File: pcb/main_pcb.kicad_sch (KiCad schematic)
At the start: 43 parts, among them J1 Conn_01x06_Socket, J4 USB_C_Receptacle_USB2.0, Q1 Si2323DS, SW1 SW_Push, SW2 SW_Push, SW3 SW_Push, U1 ESP32-H2-MINI-1, U2 LM5165Y, Y1 32.768KHz

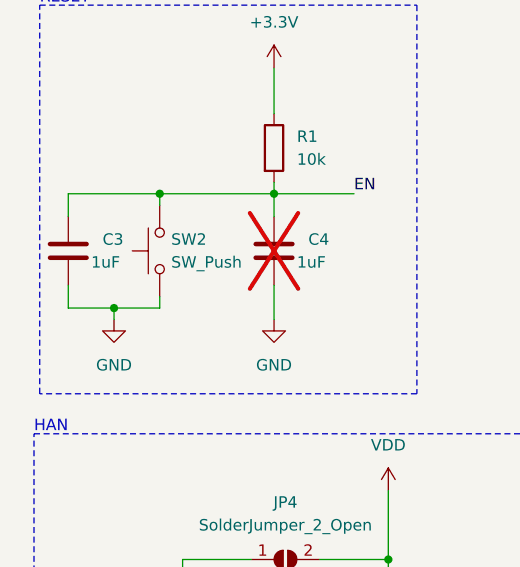
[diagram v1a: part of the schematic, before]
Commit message: Remove redundant capacitor from reset circuit
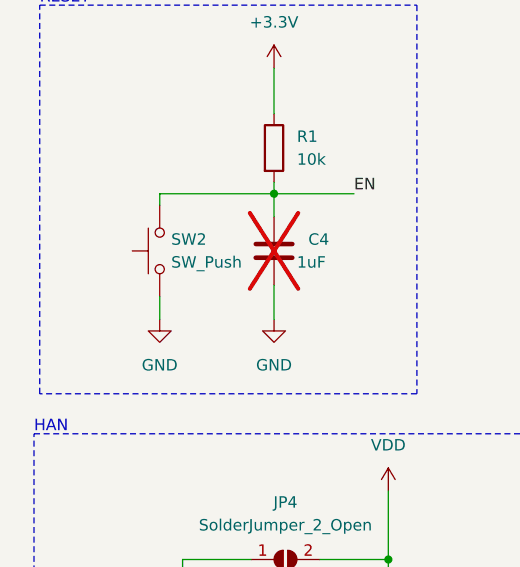
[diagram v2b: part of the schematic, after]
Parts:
- removed C3: 1uF, Capacitor_SMD:C_1206_3216Metric_Pad1.33x1.80mm_HandSolder, symbol Device:C
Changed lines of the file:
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@@
   (junction (at 165.1 176.53) (diameter 0) (color 0 0 0 0)
   )
-  (junction (at 35.56 139.7) (diameter 0) (color 0 0 0 0)
-  )
   (junction (at 111.76 72.39) (diameter 0) (color 0 0 0 0)
   )
@@
   )
   (junction (at 68.58 63.5) (diameter 0) (color 0 0 0 0)
-  )
-  (junction (at 30.48 152.4) (diameter 0) (color 0 0 0 0)
   )
   (junction (at 55.88 83.82) (diameter 0) (color 0 0 0 0)
@@
     (stroke (width 0) (type default))
   )
-  (wire (pts (xy 25.4 142.24) (xy 25.4 139.7))
-    (stroke (width 0) (type default))
-  )
   (wire (pts (xy 198.12 162.56) (xy 198.12 176.53))
     (stroke (width 0) (type default))
@@
     (stroke (width 0) (type default))
   )
-  (wire (pts (xy 25.4 139.7) (xy 35.56 139.7))
-    (stroke (width 0) (type default))
-  )
   (wire (pts (xy 250.19 134.62) (xy 256.54 134.62))
     (stroke (width 0) (type default))
@@
     (stroke (width 0) (type default))
   )
-  (wire (pts (xy 35.56 152.4) (xy 35.56 151.13))
+  (wire (pts (xy 35.56 151.13) (xy 35.56 153.67))
     (stroke (width 0) (type default))
   )
@@
     (stroke (width 0) (type default))
   )
-  (wire (pts (xy 30.48 152.4) (xy 35.56 152.4))
-    (stroke (width 0) (type default))
-  )
   (wire (pts (xy 219.71 181.61) (xy 219.71 190.5))
     (stroke (width 0) (type default))
@@
     (stroke (width 0) (type default))
   )
-  (wire (pts (xy 25.4 152.4) (xy 30.48 152.4))
-    (stroke (width 0) (type default))
-  )
   (wire (pts (xy 118.11 53.34) (xy 124.46 53.34))
     (stroke (width 0) (type default))
@@
     (stroke (width 0) (type default))
   )
-  (wire (pts (xy 25.4 149.86) (xy 25.4 152.4))
-    (stroke (width 0) (type default))
-  )
   (wire (pts (xy 201.93 189.23) (xy 191.77 189.23))
     (stroke (width 0) (type default))
@@
   )
   (wire (pts (xy 173.99 199.39) (xy 173.99 200.66))
-    (stroke (width 0) (type default))
-  )
-  (wire (pts (xy 30.48 152.4) (xy 30.48 153.67))
     (stroke (width 0) (type default))
   )
@@
     )
   )
-  (symbol (lib_id "power:GND") (at 30.48 153.67 0) (unit 1)
-    (in_bom yes) (on_board yes) (dnp no) (fields_autoplaced)
-    (property "Reference" "#PWR08" (at 30.48 160.02 0)
-      (effects (font (size 1.27 1.27)) hide)
-    )
-    (property "Value" "GND" (at 30.48 158.75 0)
-      (effects (font (size 1.27 1.27)))
-    )
-    (property "Footprint" "" (at 30.48 153.67 0)
-      (effects (font (size 1.27 1.27)) hide)
-    )
-    (property "Datasheet" "" (at 30.48 153.67 0)
+  (symbol (lib_id "power:GND") (at 35.56 153.67 0) (unit 1)
+    (in_bom yes) (on_board yes) (dnp no) (fields_autoplaced)
+    (property "Reference" "#PWR08" (at 35.56 160.02 0)
+      (effects (font (size 1.27 1.27)) hide)
+    )
+    (property "Value" "GND" (at 35.56 158.75 0)
+      (effects (font (size 1.27 1.27)))
+    )
+    (property "Footprint" "" (at 35.56 153.67 0)
+      (effects (font (size 1.27 1.27)) hide)
+    )
+    (property "Datasheet" "" (at 35.56 153.67 0)
       (effects (font (size 1.27 1.27)) hide)
     )
@@
         )
       )
-    )
-  )
-  (symbol (lib_id "Device:C") (at 25.4 146.05 0) (unit 1)
-    (in_bom yes) (on_board yes) (dnp no)
-    (property "Reference" "C3" (at 29.21 144.78 0)
-      (effects (font (size 1.27 1.27)) (justify left))
-    )
-    (property "Value" "1uF" (at 27.94 147.32 0)
-      (effects (font (size 1.27 1.27)) (justify left))
-    )
-    (property "Footprint" "Capacitor_SMD:C_1206_3216Metric_Pad1.33x1.80mm_HandSolder" (at 26.3652 149.86 0)
-      (effects (font (size 1.27 1.27)) hide)
-    )
-    (property "Datasheet" "~" (at 25.4 146.05 0)
-      (effects (font (size 1.27 1.27)) hide)
-    )
-    (pin "2")
-    (pin "1")
-    (instances
-      (project "main_pcb"
-        (path "/6204b7c2-8814-41ee-9243-5078f55f08d4"
-          (reference "C3") (unit 1)
-        )
-      )

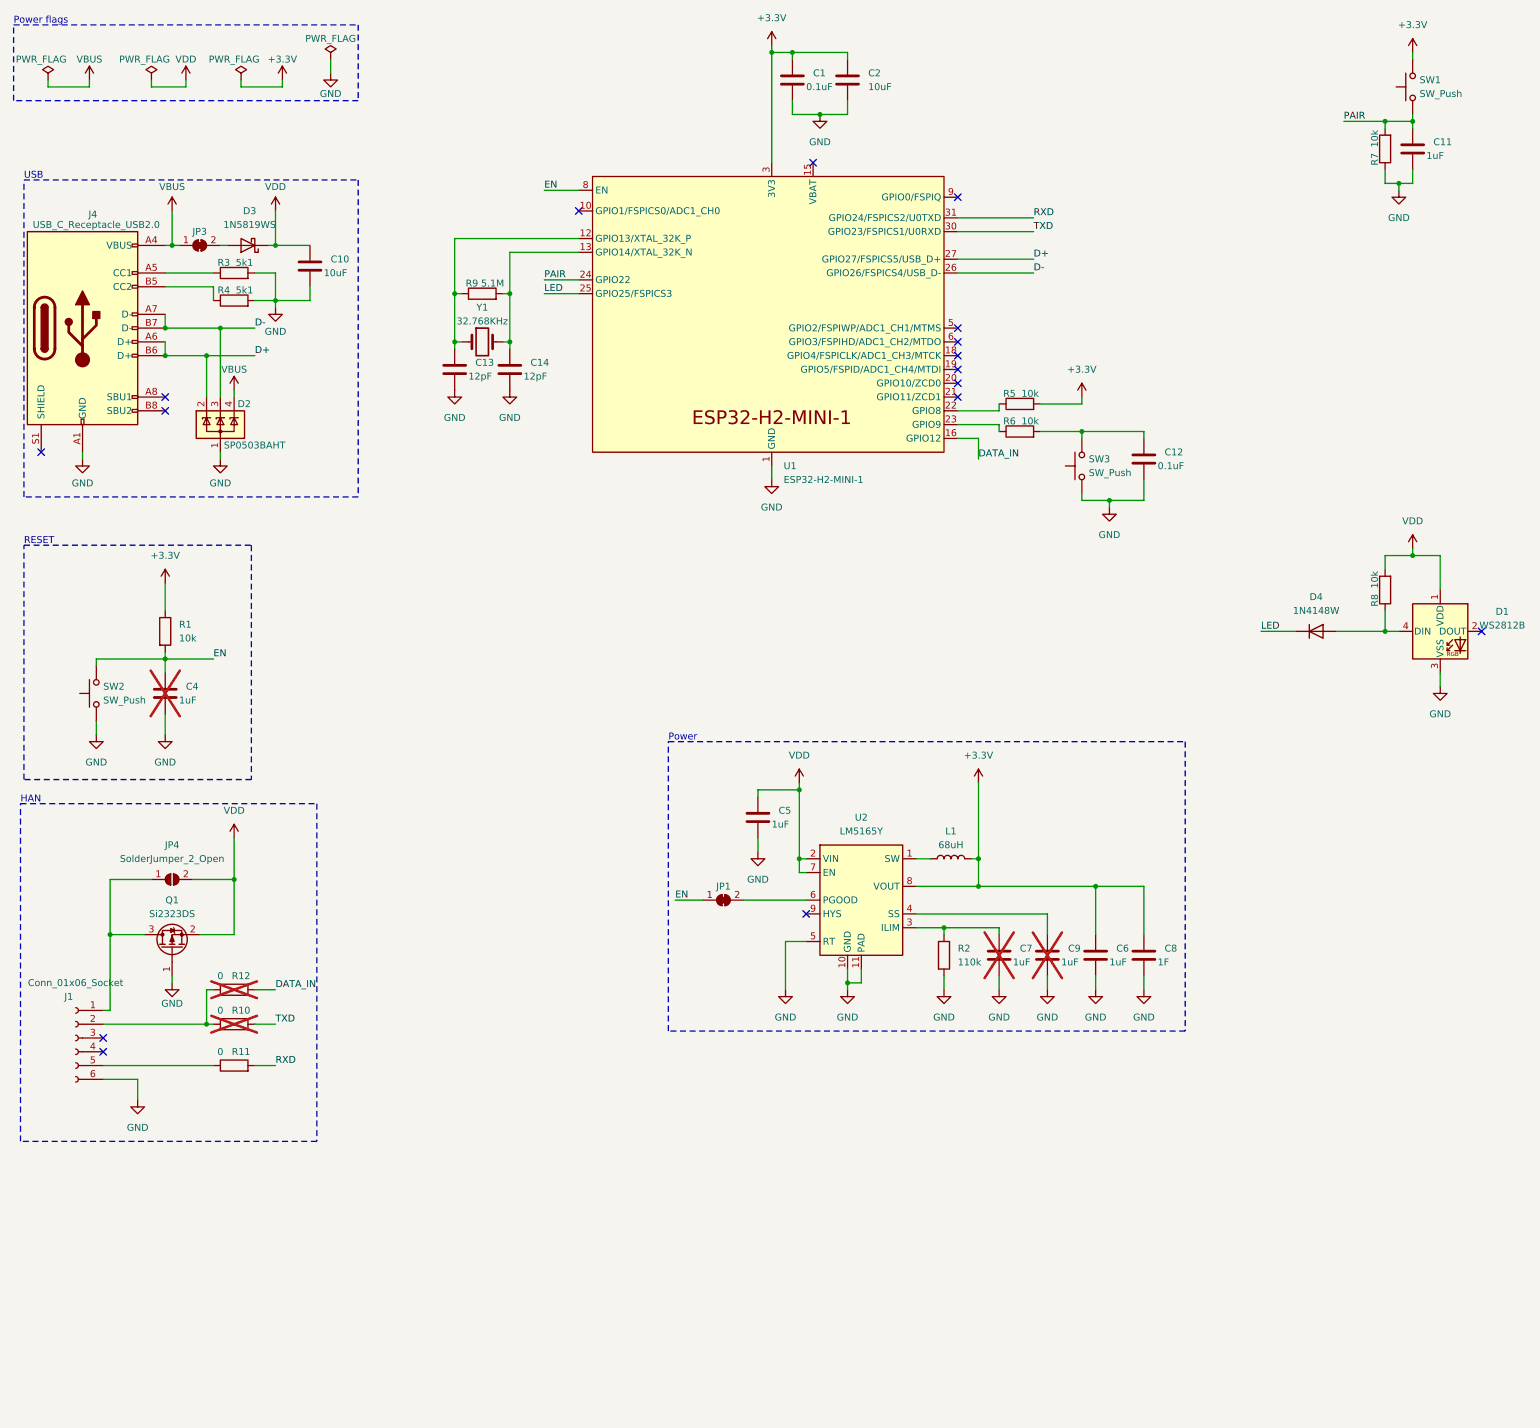
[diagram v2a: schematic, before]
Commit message: Label switches properly
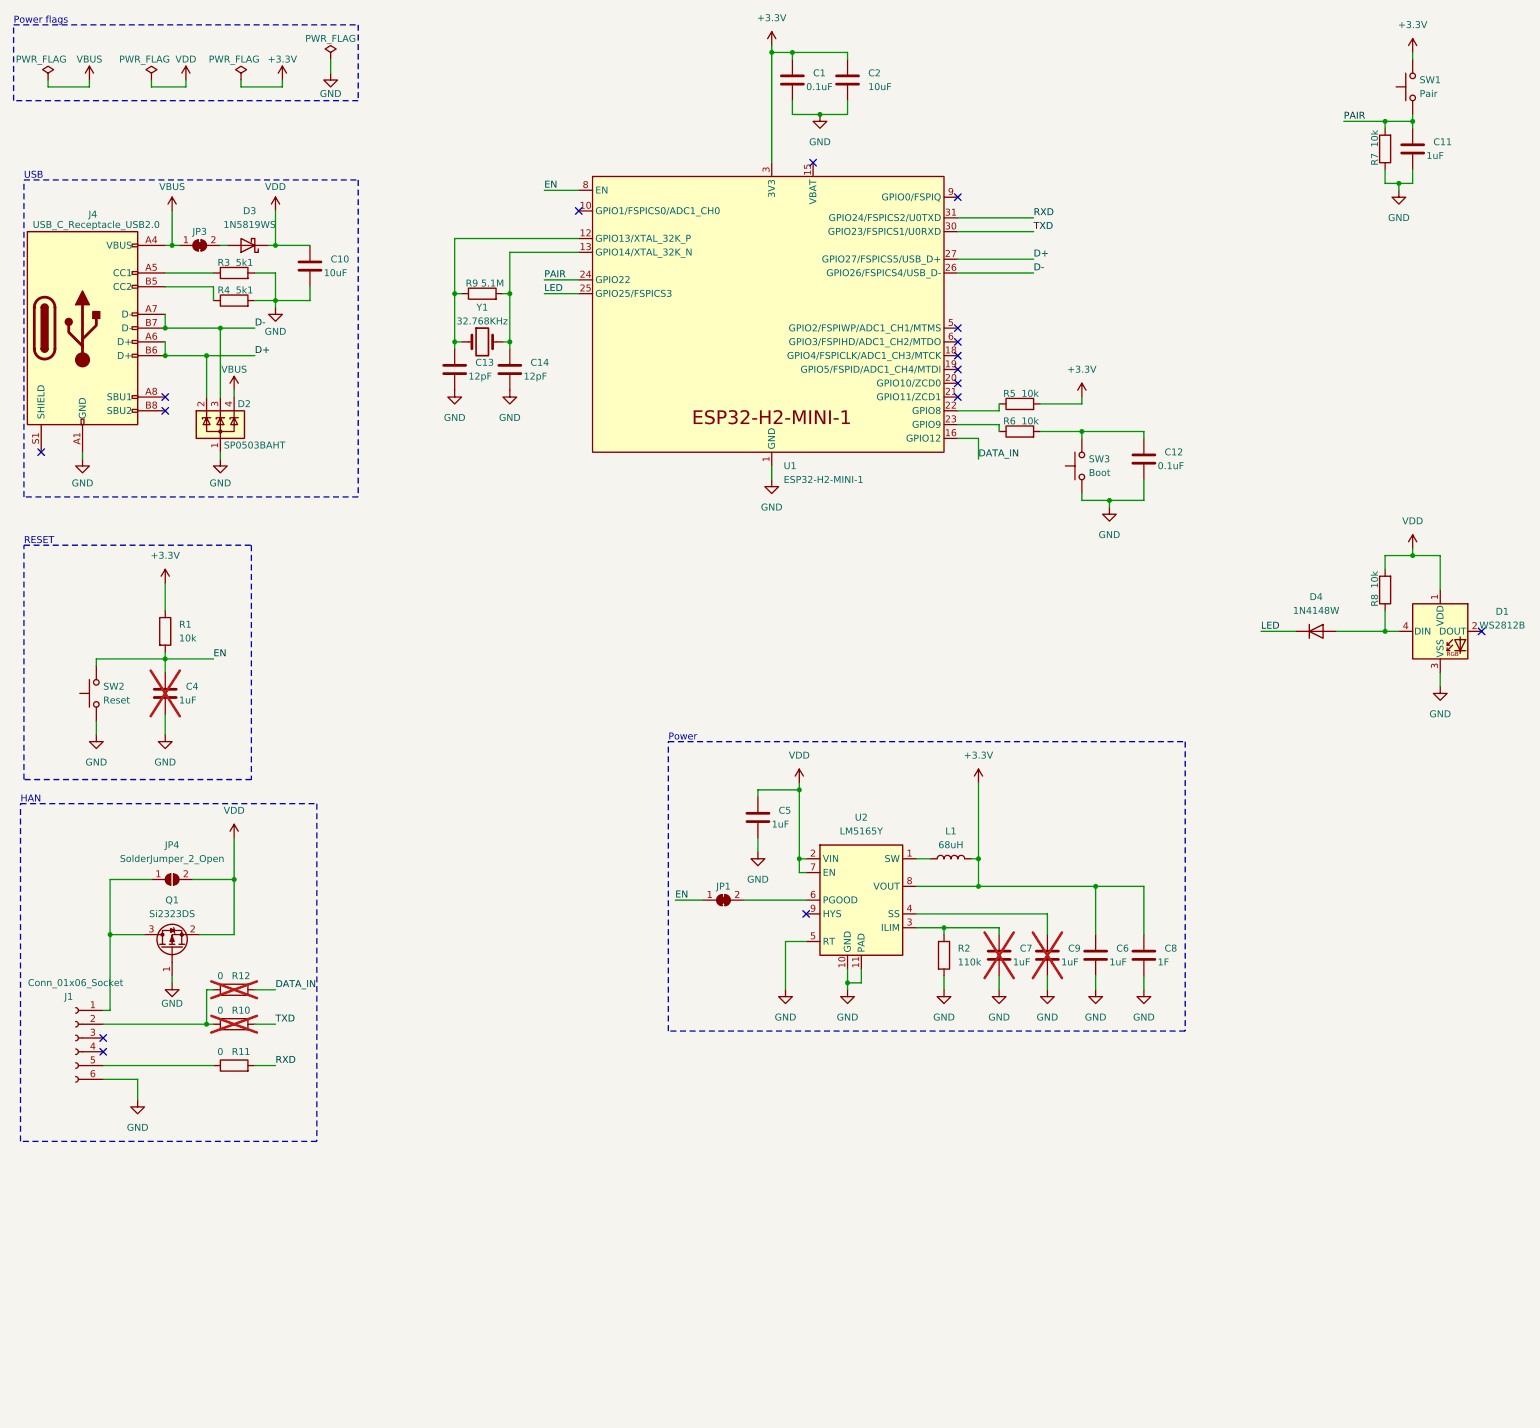
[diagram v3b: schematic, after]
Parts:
- SW1: value SW_Push -> Pair
- SW2: value SW_Push -> Reset
- SW3: value SW_Push -> Boot
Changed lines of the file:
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@@
       (effects (font (size 1.27 1.27)) (justify right))
     )
-    (property "Value" "SW_Push" (at 218.44 105.41 90)
+    (property "Value" "Boot" (at 218.44 105.41 90)
       (effects (font (size 1.27 1.27)) (justify right))
     )
@@
       (effects (font (size 1.27 1.27)) (justify right))
     )
-    (property "Value" "SW_Push" (at 279.4 35.56 90)
+    (property "Value" "Pair" (at 279.4 35.56 90)
       (effects (font (size 1.27 1.27)) (justify right))
     )
@@
       (effects (font (size 1.27 1.27)) (justify right))
     )
-    (property "Value" "SW_Push" (at 36.83 147.32 90)
+    (property "Value" "Reset" (at 36.83 147.32 90)
       (effects (font (size 1.27 1.27)) (justify right))
     )

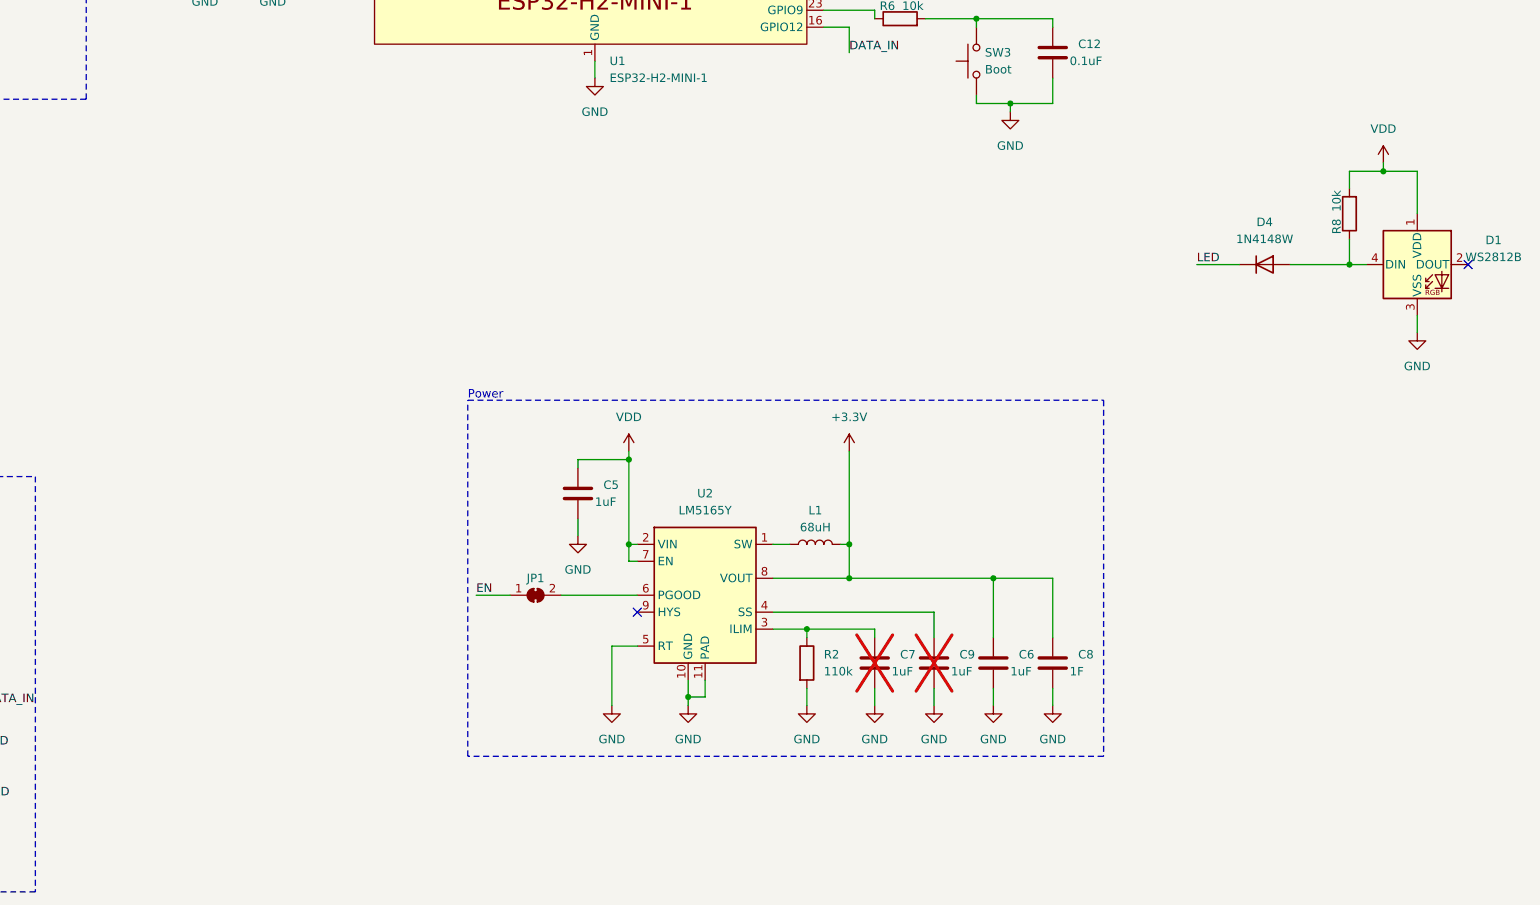
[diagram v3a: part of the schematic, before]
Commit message: Update power supply circuit
Use values recomended by TI webench power designer.
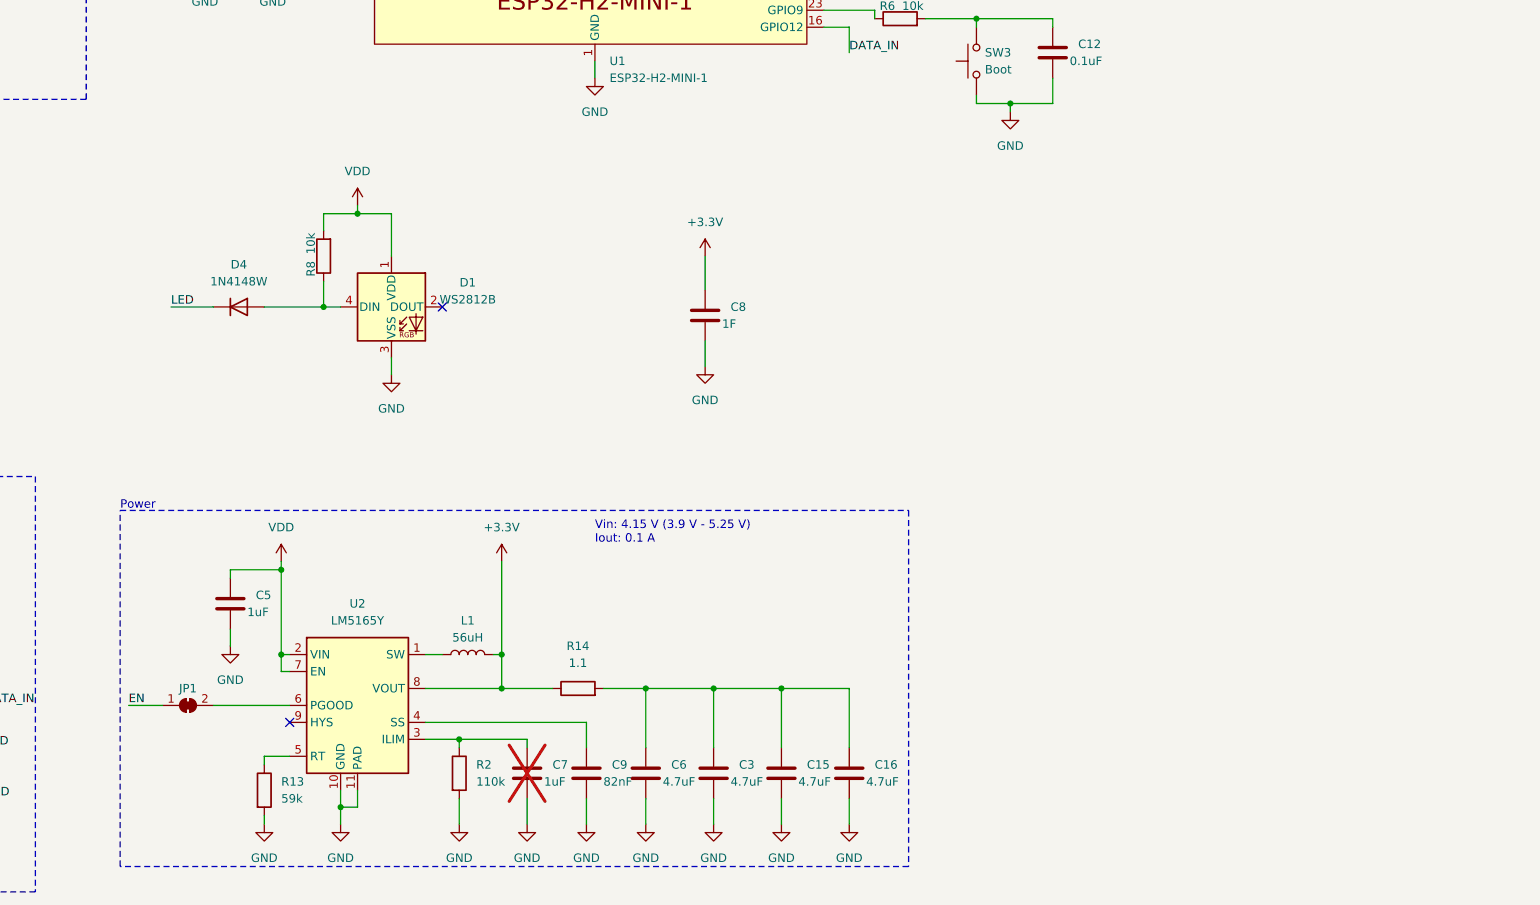
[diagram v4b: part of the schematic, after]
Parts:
- added C15, C16, C3: 4.7uF, Capacitor_SMD:C_1206_3216Metric_Pad1.33x1.80mm_HandSolder, symbol Device:C
- added R13: 59k, Resistor_SMD:R_1206_3216Metric_Pad1.30x1.75mm_HandSolder, symbol Device:R
- added R14: 1.1, Resistor_SMD:R_1206_3216Metric_Pad1.30x1.75mm_HandSolder, symbol Device:R
- C6: value 1uF -> 4.7uF
- C9: value 1uF -> 82nF; now fitted
- L1: value 68uH -> 56uH
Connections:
- net +3.3V: now also R14.1; no longer C6.1
- net GND: now also C15.2, C16.2, C3.2, R13.2; no longer U2.5 (RT)
- new net: R13.1, U2.5 (RT)
- new net: C15.1, C16.1, C3.1, C6.1, R14.2
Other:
- note added: "Vin: 4.15 V (3.9 V - 5.25 V) Iout: 0.1 A"
- moved on the sheet: C5, C6, C7, C8, D1, D4, JP1, L1, R2, R8, U2

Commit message: Improve PCB layout
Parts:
- L1: footprint Inductor_SMD:L_1206_3216Metric_Pad1.22x1.90mm_HandSolder -> Inductor_SMD:L_Wuerth_WE-PD2-Typ-L
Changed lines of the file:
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@@
       (effects (font (size 1.27 1.27)))
     )
-    (property "Footprint" "Inductor_SMD:L_1206_3216Metric_Pad1.22x1.90mm_HandSolder" (at 140.97 193.04 0)
+    (property "Footprint" "Inductor_SMD:L_Wuerth_WE-PD2-Typ-L" (at 140.97 193.04 0)
       (effects (font (size 1.27 1.27)) hide)
     )
